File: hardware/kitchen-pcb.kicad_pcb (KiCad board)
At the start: 4 copper layers, 82.6 x 82.5 mm, 85 parts, among them J1 MEM2075-00-140-01-A, J2 Conn_02x02_Odd_Even, J3 Conn_01x06, J4 S3B-XH-SM4-TB_LF__SN_, J5 DCJ200-10-A-K1-K, J6 USB4105-GF-A, Q1 TEMT6000X01, SW1 RA1113112R, SW2 SW_Push, SW3 SW_Push, U1 SHT30-DIS-B, U2 MX25L3233FM2I-08G, U3 NCP1117ST33T3G, U4 ESP32-S3-WROOM-1-N8R8, U5 USBLC6-2SC6

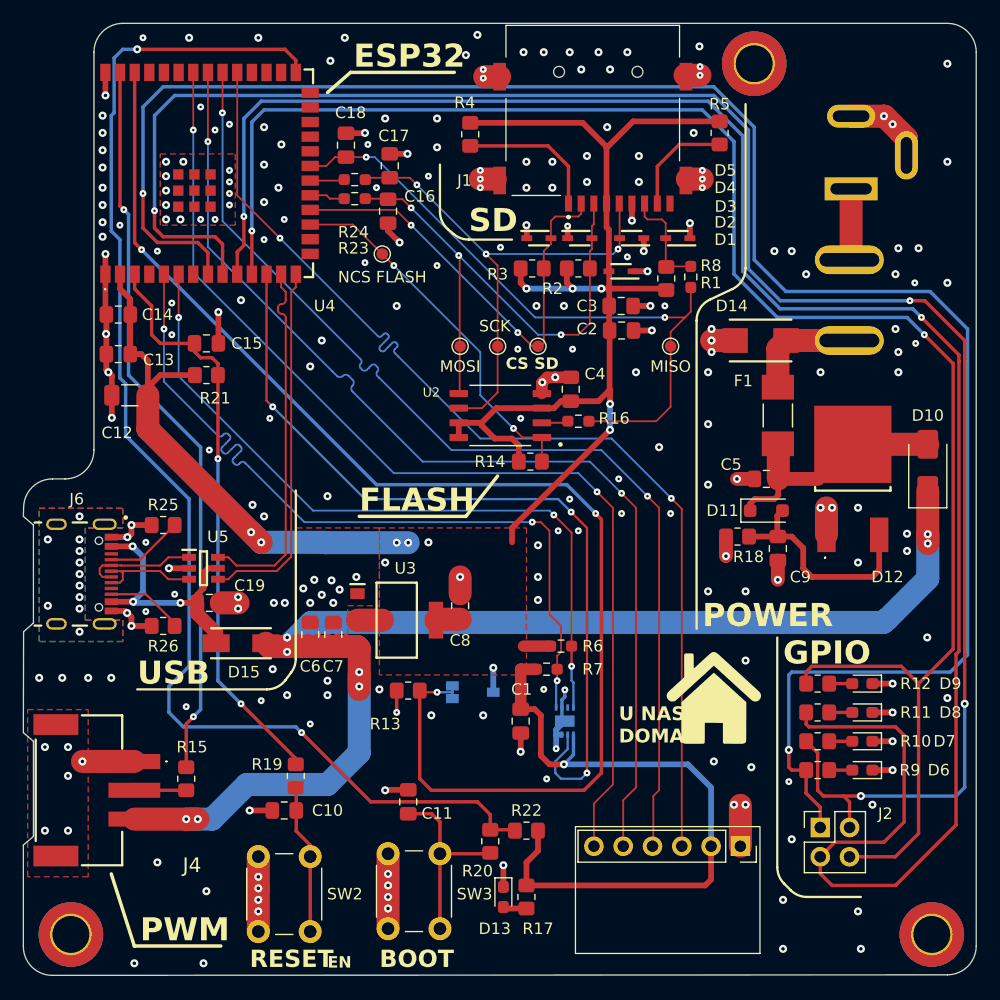
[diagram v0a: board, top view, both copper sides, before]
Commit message: PCB v0.2 (Changed GPIO routing, better power distribution)
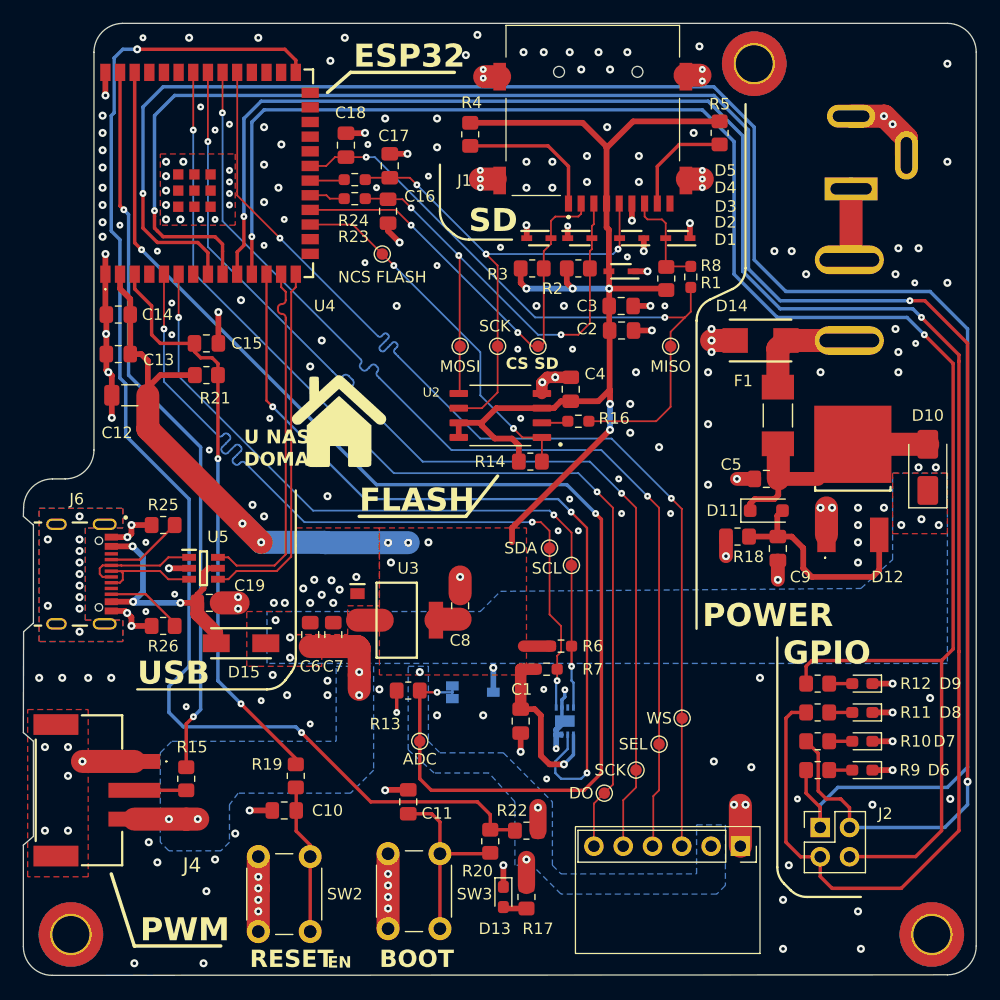
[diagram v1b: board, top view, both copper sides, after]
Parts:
- added TP1: SDA, TestPoint:TestPoint_Pad_D1.0mm, F.Cu at (143.0, 104.0)
- added TP11: DO, TestPoint:TestPoint_Pad_D1.0mm, F.Cu at (147.8, 125.2)
- added TP12: ADC, TestPoint:TestPoint_Pad_D1.0mm, F.Cu at (131.8, 120.8)
- added TP3: SCL, TestPoint:TestPoint_Pad_D1.0mm, F.Cu at (144.9, 105.5)
- added TP5: WS, TestPoint:TestPoint_Pad_D1.0mm, F.Cu at (154.5, 118.8)
- added TP7: SEL, TestPoint:TestPoint_Pad_D1.0mm, F.Cu at (152.5, 121.0)
- added TP9: SCK, TestPoint:TestPoint_Pad_D1.0mm, F.Cu at (150.5, 123.2)
- moved G*** 40.4 mm to (124.8, 93.0)
- renumbered TP5 to TP10, TP1 to TP2, TP2 to TP4, TP3 to TP6, TP4 to TP8
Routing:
- net +5V: track 107.9 -> 13.4 mm, vias 8 -> 10
- net +3V3: track 214.2 -> 176.6 mm, vias 11 -> 14
- net GPIO17: track 175.0 -> 166.0 mm
- net GPIO18: track 150.7 -> 153.6 mm
- net GPIO16: track 165.3 -> 166.9 mm, vias 4 -> 3
- net GPIO15: vias 2 -> 1
- net GND: vias 252 -> 255
- added copper zone on B.Cu, net +3V3
- added copper zone on B.Cu, net +5V
- added copper zone on F.Cu, net +5V

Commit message: v0.3.1 Changed board stackup and impedance controlled traces
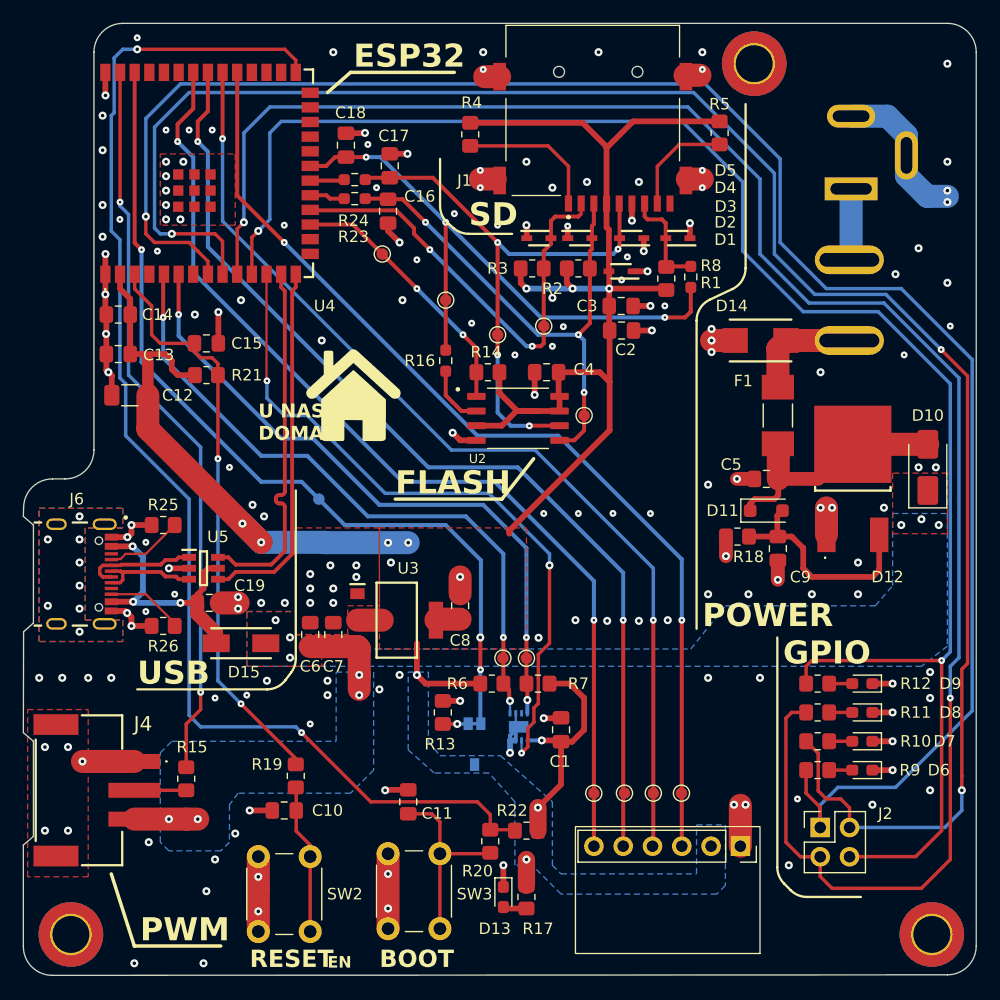
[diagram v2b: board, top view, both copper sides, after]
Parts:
- D1, D2, D3, D4, D5: value PESD3V3L1BA,115 -> UCLAMP3301D.TCT
- D10, D15: value D_Schottky -> B320AE-13
- R6, R7: value 4k7 -> 5k1; footprint Resistor_SMD:R_0603_1608Metric_Pad0.98x0.95mm_HandSolder -> Resistor_SMD:R_0805_2012Metric_Pad1.20x1.40mm_HandSolder
- TP1: value SDA -> Test_SCK
- TP10: value NCS FLASH -> Test_NCS_FLASH
- TP11: value DO -> Test_CS_SD
- TP12: value ADC -> Test_NCS_FLASH; moved to B.Cu
- TP2: value SCK -> Test_SCK
- TP3: value SCL -> Test_MISO
- TP4: value MISO -> Test_MISO
- TP5: value WS -> Test_SCK
- TP6: value MOSI -> Test_MOSI
- TP7: value SEL -> Test_MISO
- TP8: value CS SD -> Test_CS_SD
- TP9: value SCK -> Test_MOSI
- moved TP12 22.8 mm to (123.0, 99.8)
- moved TP4 19.9 mm to (134.0, 82.5)
- moved R16 12.6 mm to (134.0, 87.8), turned to 90 degrees
- moved TP6 12.3 mm to (146.0, 92.5)
- moved TP1 10.4 mm to (139.0, 113.5)
- moved TP3 8.94 mm to (141.0, 113.5)
- moved R14 8.58 mm to (137.7, 88.8), turned to 180 degrees
- moved TP5 6.50 mm to (154.4, 125.2)
- moved R7 4.91 mm to (138.0, 115.8)
- moved Q1 4.50 mm to (136.5, 121.0), turned to -90 degrees
- moved TP7 4.28 mm to (152.0, 125.2)
- moved U1 4.03 mm to (140.3, 119.5)
- moved R6 3.82 mm to (142.0, 115.8), turned to 0 degrees
- moved C1 3.58 mm to (144.0, 119.8), turned to -90 degrees
- moved R13 3.55 mm to (133.8, 118.2), turned to 90 degrees
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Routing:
- net LIGHT_ADC2: track 115.6 -> 79.6 mm, vias 3 -> 4
- net TEMP_HUM_NRST: track 71.5 -> 60.2 mm
- net TEMP_HUM_I2C_SDA: track 68.9 -> 57.9 mm
- net SPI2_NCS_FLASH: track 32.3 -> 23.3 mm
- net +3V3: track 176.6 -> 184.5 mm, vias 14 -> 11
- net GPIO15: track 166.1 -> 159.0 mm
- net GPIO18: track 153.6 -> 146.7 mm
- net TEMP_HUM_I2C_SCL: track 63.8 -> 57.5 mm
- net MIC_I2S_WS: track 93.2 -> 87.2 mm
- net MIC_I2S_SEL: track 92.2 -> 87.0 mm
- net SPI2_MISO: track 57.3 -> 52.1 mm, vias 2 -> 3
- net MIC_I2S_SCK: track 92.2 -> 87.3 mm
- net GPIO16: track 166.9 -> 162.0 mm
- net MIC_I2S_DO: track 92.2 -> 87.6 mm
- net GPIO17: track 166.0 -> 161.7 mm
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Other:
- board text added: "JLCJLCJLCJLC"
- board text added: "S/N"

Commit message: v0.4 - ORDERED
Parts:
- moved TP12 13.4 mm to (135.8, 103.8)
- moved R21 4.04 mm to (111.8, 85.2), turned to -90 degrees
- moved C15 1.41 mm to (114.2, 85.2), turned to -90 degrees
- moved H3 0.50 mm to (160.2, 62.0)
- moved TP9 0.12 mm to (149.4, 125.2)
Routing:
- net +3V3: track 184.5 -> 187.9 mm
- net GPIO18: track 146.7 -> 148.4 mm
- net GND: track 121.1 -> 119.8 mm, vias 184 -> 200
- net SPI2_MISO: track 52.1 -> 53.4 mm
- net GPIO17: track 161.7 -> 162.9 mm
- net /ESP32/EN: track 50.6 -> 49.6 mm
- net GPIO15: track 159.0 -> 159.7 mm
- net LIGHT_ADC2: track 79.6 -> 80.2 mm
- net GPIO16: track 162.0 -> 162.6 mm

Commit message: Working prototype, PCB prototype revision done
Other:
- board text added: "R19 replaced with 0 ohm jumer (caused EN pin to fluctuate)"
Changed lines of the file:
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@@
+		)
+	)
+	(gr_text "R19 replaced with 0 ohm jumer (caused EN pin to fluctuate)"
+		(at 97.5 145 0)
+		(layer "Cmts.User")
+		(effects
+			(font
+				(size 1 1)
+				(thickness 0.15)
+			)
+			(justify left bottom)
 		)
 	)

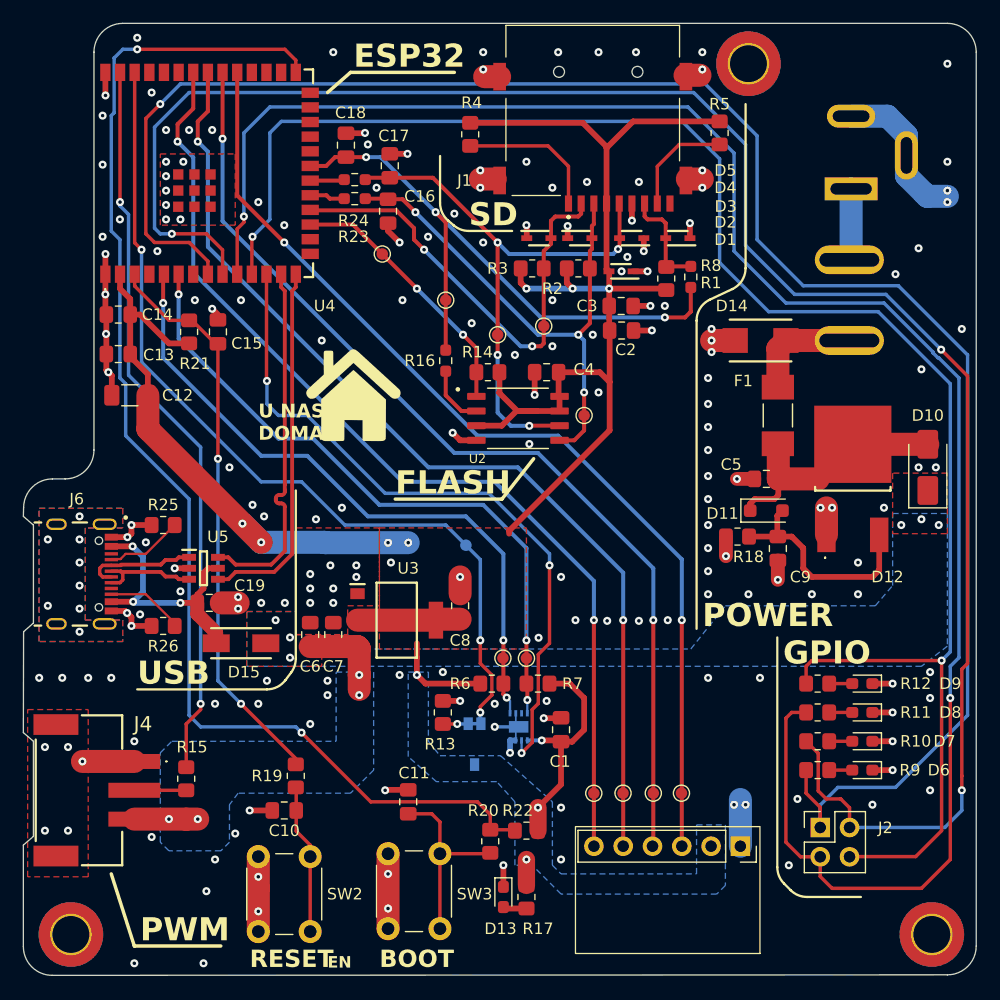
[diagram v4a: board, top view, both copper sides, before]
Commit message: rought first draft - silkscrren, crossover problems, modify for easier soldering
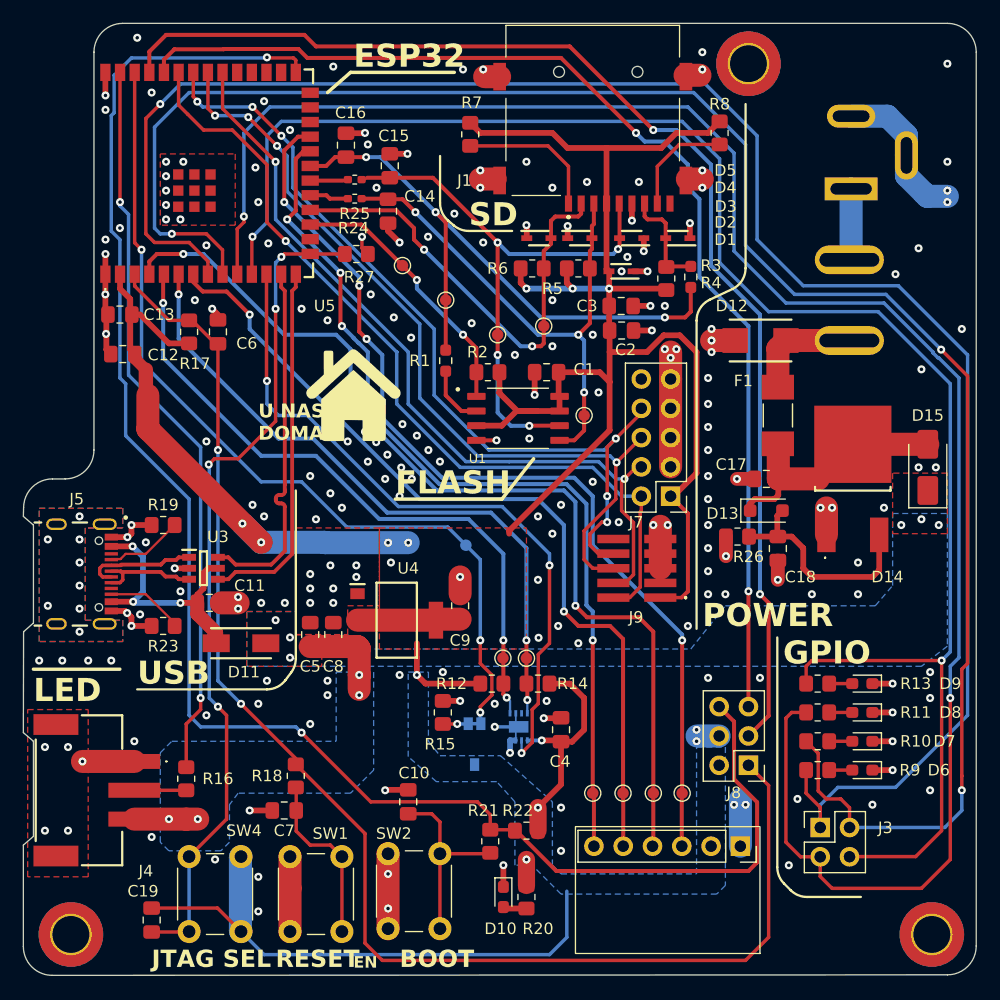
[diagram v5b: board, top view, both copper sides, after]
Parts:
- removed the C12 at (106.6, 90.8)
- added C19: 100n, Capacitor_SMD:C_0805_2012Metric_Pad1.18x1.45mm_HandSolder, F.Cu at (108.5, 136.2)
- added J7: Conn_02x05_Odd_Even, Connector_PinHeader_2.54mm:PinHeader_2x05_P2.54mm_Vertical, F.Cu at (153.5, 99.5)
- added J8: Conn_02x03_Odd_Even, Connector_PinHeader_2.54mm:PinHeader_2x03_P2.54mm_Vertical, F.Cu at (160.2, 122.8)
- added J9: Conn_02x05_Odd_Even, ESP32-project-footprints:FTSH10501LDVK, F.Cu at (152.6, 105.8)
- added R27: 10k, Resistor_SMD:R_0805_2012Metric_Pad1.20x1.40mm_HandSolder, F.Cu at (126.2, 78.5)
- added SW4: SW_Push, Button_Switch_THT:SW_PUSH_6mm_H9.5mm, F.Cu at (116.2, 130.8)
- R24: renamed from R23; footprint Resistor_SMD:R_0603_1608Metric_Pad0.98x0.95mm_HandSolder -> Resistor_SMD:R_0402_1005Metric_Pad0.72x0.64mm_HandSolder
- R25: renamed from R24; footprint Resistor_SMD:R_0603_1608Metric_Pad0.98x0.95mm_HandSolder -> Resistor_SMD:R_0402_1005Metric_Pad0.72x0.64mm_HandSolder
- moved SW1 2.75 mm to (120.5, 137.2)
- moved TP11 2.02 mm to (130.2, 79.5)
- moved C12 0.39 mm to (106.0, 87.2)
- moved C13 0.14 mm to (105.8, 83.8)
- moved TP6 0.09 mm to (146.8, 125.2)
- moved TP3 0.06 mm to (154.5, 125.2)
- renumbered C4 to C1, C11 to C10, C19 to C11, C13 to C12, C14 to C13, C16 to C14, C17 to C15, C18 to C16, C5 to C17, C9 to C18, C1 to C4, C6 to C5, C15 to C6, C10 to C7, C7 to C8, C8 to C9, D13 to D10, D15 to D11, D14 to D12, D11 to D13, D12 to D14, D10 to D15, J3 to J2, J2 to J3, J6 to J5, J5 to J6, R16 to R1, R6 to R12, R12 to R13, R7 to R14, R13 to R15, R15 to R16, R21 to R17, R19 to R18, R25 to R19, R14 to R2, R17 to R20, R20 to R21, R26 to R23, R18 to R26, R8 to R3, R1 to R4, R2 to R5, R3 to R6, R4 to R7, R5 to R8, SW2 to SW1, SW3 to SW2, SW1 to SW3, TP8 to TP10, TP10 to TP11, TP3 to TP2, TP5 to TP3, TP7 to TP4, TP9 to TP5, TP11 to TP6, TP2 to TP7, TP4 to TP8, TP6 to TP9, U2 to U1, U1 to U2, U5 to U3, U3 to U4, U4 to U5
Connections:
- net /ESP32/BOOT renamed BOOT
- net /ESP32/EN renamed EN
- U5 pad 15: unconnected-(U4-IO3-Pad15) -> JTAG_SEL
- U5 pad 22: unconnected-(U4-IO14-Pad22) -> MIC_I2S_DO
- U5 pad 23: unconnected-(U4-IO21-Pad23) -> MIC_I2S_WS
- U5 pad 31: MIC_I2S_WS -> unconnected-(U5-IO38-Pad31)
- U5 pad 32: MIC_I2S_SEL -> MTCK
- U5 pad 33: MIC_I2S_SCK -> MTDO
- U5 pad 34: MIC_I2S_DO -> MTDI
- U5 pad 35: unconnected-(U4-IO42-Pad35) -> MTMS
- U5 pad 36: unconnected-(U4-RXD0-Pad36) -> RX
- U5 pad 37: unconnected-(U4-TXD0-Pad37) -> TX
- U5 pad 4: unconnected-(U4-IO4-Pad4) -> MIC_I2S_SEL
- U5 pad 7: unconnected-(U4-IO7-Pad7) -> MIC_I2S_SCK
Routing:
- net TX: track 0.00 -> 108.1 mm, vias 0 -> 2
- net RX: track 0.00 -> 100.2 mm, vias 0 -> 2
- net +3V3: track 187.9 -> 270.4 mm
- net MTDI: track 0.00 -> 73.8 mm, vias 0 -> 6
- net MTMS: track 0.00 -> 73.2 mm, vias 0 -> 1
- net JTAG_SEL: track 0.00 -> 73.2 mm, vias 0 -> 4
- net MTDO: track 0.00 -> 72.3 mm, vias 0 -> 4
- net MTCK: track 0.00 -> 70.1 mm, vias 0 -> 2
- net EN: track 49.6 -> 119.7 mm
- net BOOT: track 110.6 -> 146.7 mm
- net GND: track 119.8 -> 134.2 mm, vias 200 -> 221
- net MIC_I2S_SCK: track 87.3 -> 73.9 mm
- net MIC_I2S_DO: track 87.6 -> 79.1 mm, vias 2 -> 4
- net MIC_I2S_WS: track 87.2 -> 84.1 mm, vias 2 -> 4
- net Net-(C7-Pad2): track 13.1 -> 15.2 mm
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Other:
- board text added: "JTAG SEL"
- board text added: "LED"
- board text removed: "PWM"
